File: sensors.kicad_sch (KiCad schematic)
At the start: 328 parts, among them K1 DRV5055A3xDBZxQ1, K10 DRV5055A3xDBZxQ1, K11 DRV5055A3xDBZxQ1, K12 DRV5055A3xDBZxQ1, K13 DRV5055A3xDBZxQ1, K14 DRV5055A3xDBZxQ1, K15 DRV5055A3xDBZxQ1, K16 DRV5055A3xDBZxQ1, K17 DRV5055A3xDBZxQ1, K18 DRV5055A3xDBZxQ1, K19 DRV5055A3xDBZxQ1, K2 DRV5055A3xDBZxQ1, K20 DRV5055A3xDBZxQ1, K21 DRV5055A3xDBZxQ1, K22 DRV5055A3xDBZxQ1, K23 DRV5055A3xDBZxQ1, K24 DRV5055A3xDBZxQ1, K25 DRV5055A3xDBZxQ1, K26 DRV5055A3xDBZxQ1, K27 DRV5055A3xDBZxQ1, K28 DRV5055A3xDBZxQ1, K29 DRV5055A3xDBZxQ1, K3 DRV5055A3xDBZxQ1, K30 DRV5055A3xDBZxQ1, K31 DRV5055A3xDBZxQ1, K32 DRV5055A3xDBZxQ1, K33 DRV5055A3xDBZxQ1, K34 DRV5055A3xDBZxQ1, K35 DRV5055A3xDBZxQ1, K36 DRV5055A3xDBZxQ1, K37 DRV5055A3xDBZxQ1, K38 DRV5055A3xDBZxQ1, K39 DRV5055A3xDBZxQ1, K4 DRV5055A3xDBZxQ1, K40 DRV5055A3xDBZxQ1, K41 DRV5055A3xDBZxQ1, K42 DRV5055A3xDBZxQ1, K43 DRV5055A3xDBZxQ1, K44 DRV5055A3xDBZxQ1, K45 DRV5055A3xDBZxQ1, K46 DRV5055A3xDBZxQ1, K47 DRV5055A3xDBZxQ1, K48 DRV5055A3xDBZxQ1, K49 DRV5055A3xDBZxQ1, K5 DRV5055A3xDBZxQ1, K50 DRV5055A3xDBZxQ1, K51 DRV5055A3xDBZxQ1, K52 DRV5055A3xDBZxQ1, K53 DRV5055A3xDBZxQ1, K54 DRV5055A3xDBZxQ1, K55 DRV5055A3xDBZxQ1, K56 DRV5055A3xDBZxQ1, K57 DRV5055A3xDBZxQ1, K58 DRV5055A3xDBZxQ1, K59 DRV5055A3xDBZxQ1, K6 DRV5055A3xDBZxQ1, K60 DRV5055A3xDBZxQ1, K61 DRV5055A3xDBZxQ1, K62 DRV5055A3xDBZxQ1, K63 DRV5055A3xDBZxQ1, K64 DRV5055A3xDBZxQ1, K65 DRV5055A3xDBZxQ1, K66 DRV5055A3xDBZxQ1, K67 DRV5055A3xDBZxQ1, K68 DRV5055A3xDBZxQ1, K69 DRV5055A3xDBZxQ1, K7 DRV5055A3xDBZxQ1, K70 DRV5055A3xDBZxQ1, K71 DRV5055A3xDBZxQ1, K72 DRV5055A3xDBZxQ1, K73 DRV5055A3xDBZxQ1, K74 DRV5055A3xDBZxQ1, K75 DRV5055A3xDBZxQ1, K76 DRV5055A3xDBZxQ1, K77 DRV5055A3xDBZxQ1, K78 DRV5055A3xDBZxQ1, K79 DRV5055A3xDBZxQ1, K8 DRV5055A3xDBZxQ1, K80 DRV5055A3xDBZxQ1, K81 DRV5055A3xDBZxQ1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

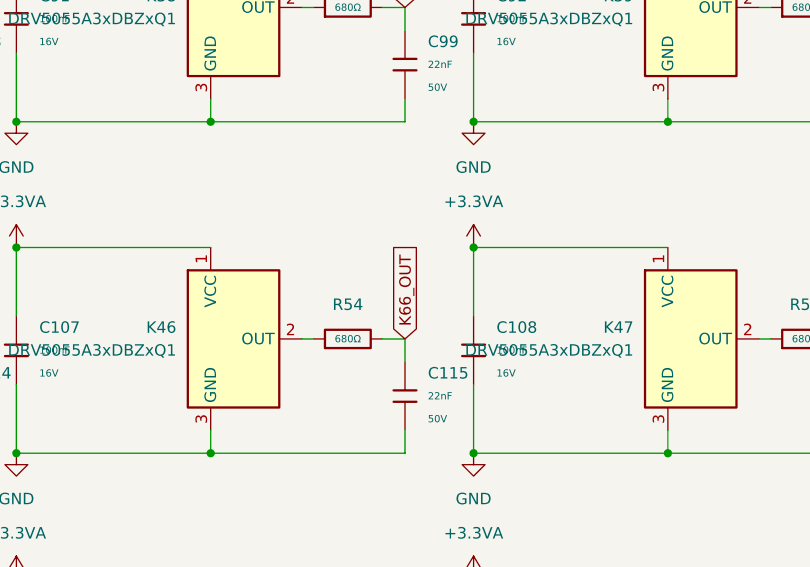
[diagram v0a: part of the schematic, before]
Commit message: place sensors capacitor
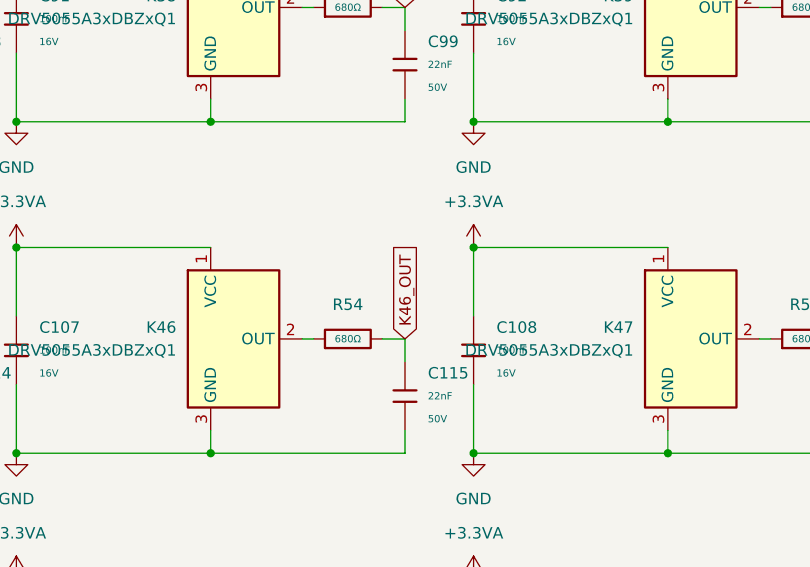
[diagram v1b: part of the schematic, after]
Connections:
- net K66_OUT: no longer C115.2, R54.2
- new net K46_OUT: C115.2, R54.2
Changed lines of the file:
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@@
 		)
 	)
-	(global_label "K66_OUT"
+	(global_label "K46_OUT"
 		(shape input)
 		(at 316.23 217.17 90)

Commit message: lcsc part
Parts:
- K1, K10, K11, K12, K13, K14, K15, K16, K17, K18, K19, K2, K20, K21, K22, K23, K24, K25, K26, K27, K28, K29, K3, K30, K31, K32, K33, K34, K35, K36, K37, K38, K39, K4, K40, K41, K42, K43, K44, K45, K46, K47, K48, K49, K5, K50, K51, K52, K53, K54, K55, K56, K57, K58, K59, K6, K60, K61, K62, K63, K64, K65, K66, K67, K68, K69, K7, K70, K71, K72, K73, K74, K75, K76, K77, K78, K79, K8, K80, K81, K82, K9: LCSC (none) -> C266128
